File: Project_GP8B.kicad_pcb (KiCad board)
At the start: 4 copper layers, 133 x 93 mm, 103 parts, among them IC1 XC2C256-VQ100, J1 ALU_JTAG, J2 TE_Eurocard_96pole, J3 5530843-2, J4 UnusedPins_Connector, J5 ALU_PINS, U1 74AHC05, U10 74AHC1G04, U11 CD74AC238, U12 74AHC1G04, U13 CD74AC238, U14 74AHC08, U15 CD74AC238, U16 74AHC08, U17 74AHC138, U18 74HC165, U19 74AHCT244, U2 74AHC05, U20 74AHCT244, U21 74AHCT244, U22 74AHCT244, U23 74AHCT244, U24 74AHC273, U25 74AHCT595, U26 74AHC273, U27 74AHC273, U28 TPS7A0518PDBZR, U29 74AHC273, U3 74AHC1G04, U30 SN74LVC8T245DW, U31 74AHC273, U32 SN74AVC4T245D, U33 74AHC273, U35 74AHC273, U36 74AHC1G04, U37 74AHC273, U38 74AHC374, U39 74AHC1G04, U4 74AHC1G04, U5 74AHC05, U6 74AHC273, U7 74AHCT273, U8 74HC163, U9 CD74AC238

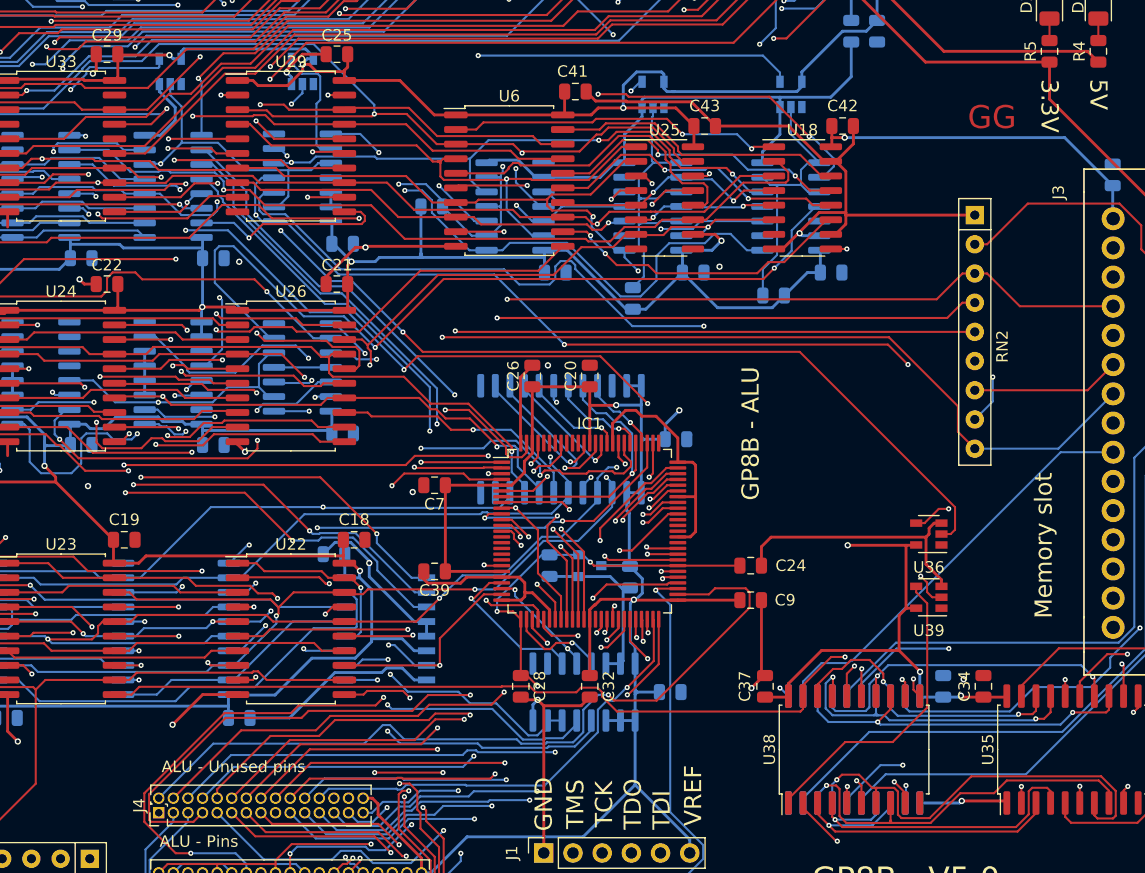
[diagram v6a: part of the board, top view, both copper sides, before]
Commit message: Apply MM1 memory standard, and shared power pin symbol fix
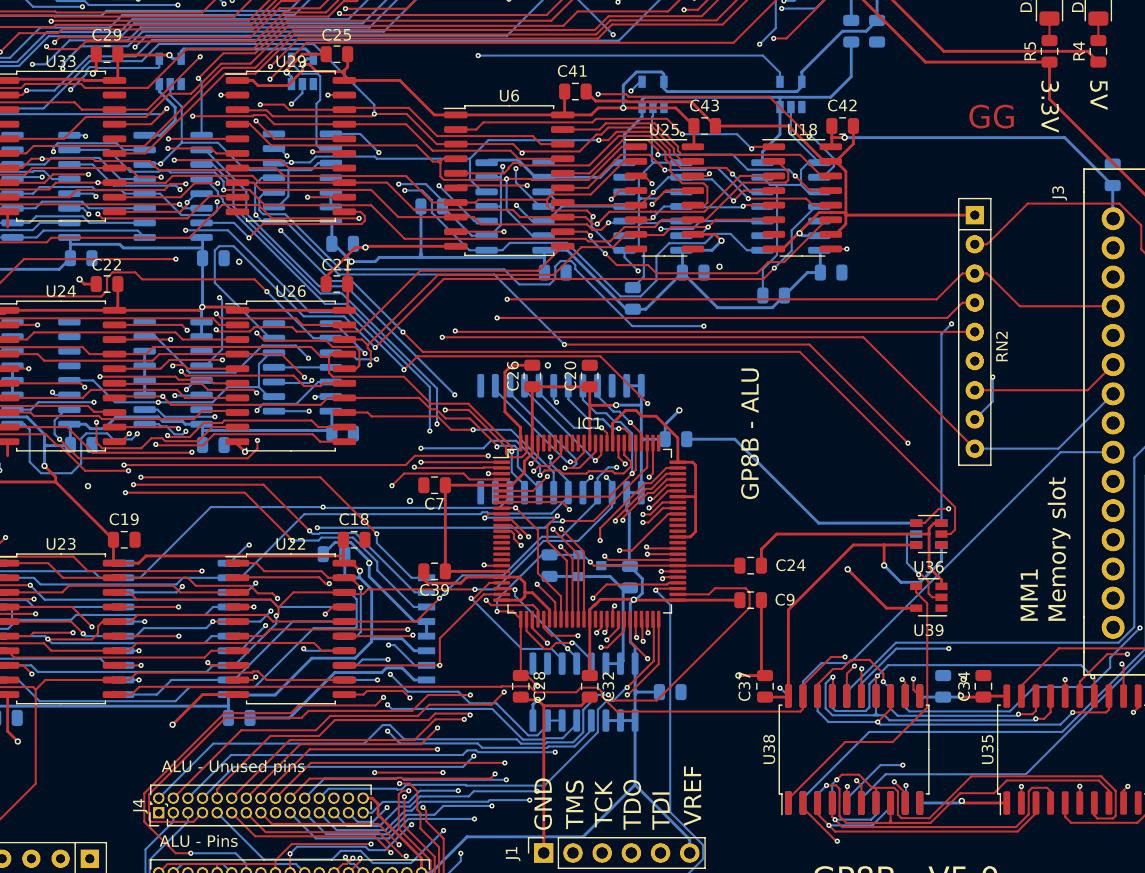
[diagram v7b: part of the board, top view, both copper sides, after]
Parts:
- removed G***: LOGO, QRCode:QRCode
- added U34: 74LVC1G34, Package_TO_SOT_SMD:SOT-23-5, B.Cu at (168.5, 89.8)
- J3: value 5530843-2 -> MM1_5530843-2
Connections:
- C34 pad 1: +5V -> +3V3
- C35 pad 1: +5V -> +3V3
- C37 pad 2: +5V -> +3V3
- J3 pad 27: /RAM_OE_CONTROL -> /RAM/B_RAM_~OE
- U35 pad 1: +5V -> +3V3
- U35 pad 20: +5V -> +3V3
- U36 pad 5: +5V -> +3V3
- U37 pad 1: +5V -> +3V3
- U37 pad 20: +5V -> +3V3
- U38 pad 20: +5V -> +3V3
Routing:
- net +3V3: track 238.9 -> 337.7 mm, vias 3 -> 6
- net +5V: track 660.9 -> 610.3 mm, vias 13 -> 10
- net /RAM/B_RAM_~OE: track 0.00 -> 43.5 mm, vias 0 -> 1
- net /RAM_OE_CONTROL: track 158.4 -> 128.7 mm
- net GND: track 410.5 -> 436.5 mm
- net /NumberSelect/RAMDATA_0: track 160.5 -> 159.2 mm
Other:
- board text added: "MM1 Memory slot"
- board text removed: "Memory slot"

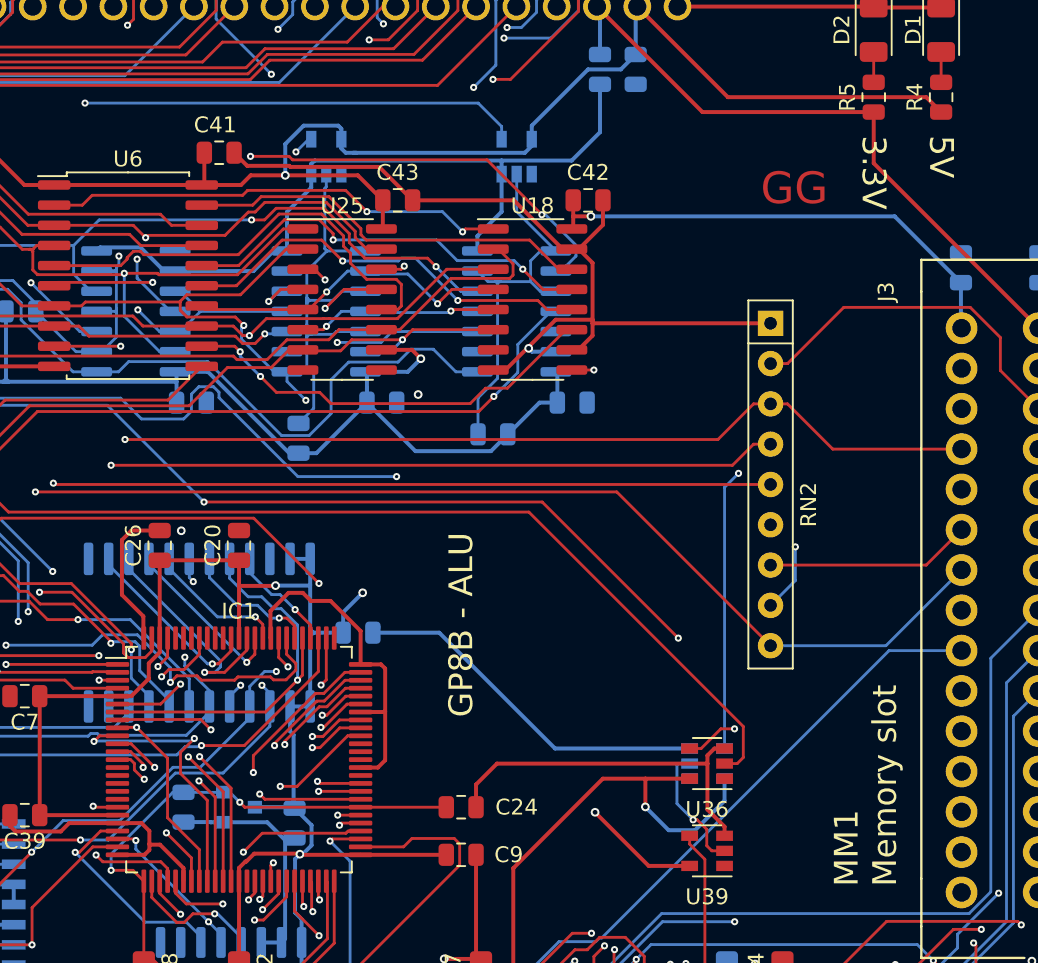
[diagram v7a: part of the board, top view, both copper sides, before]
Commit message: Revert SPI 4bits problem work-around (finally this fixed nothing)
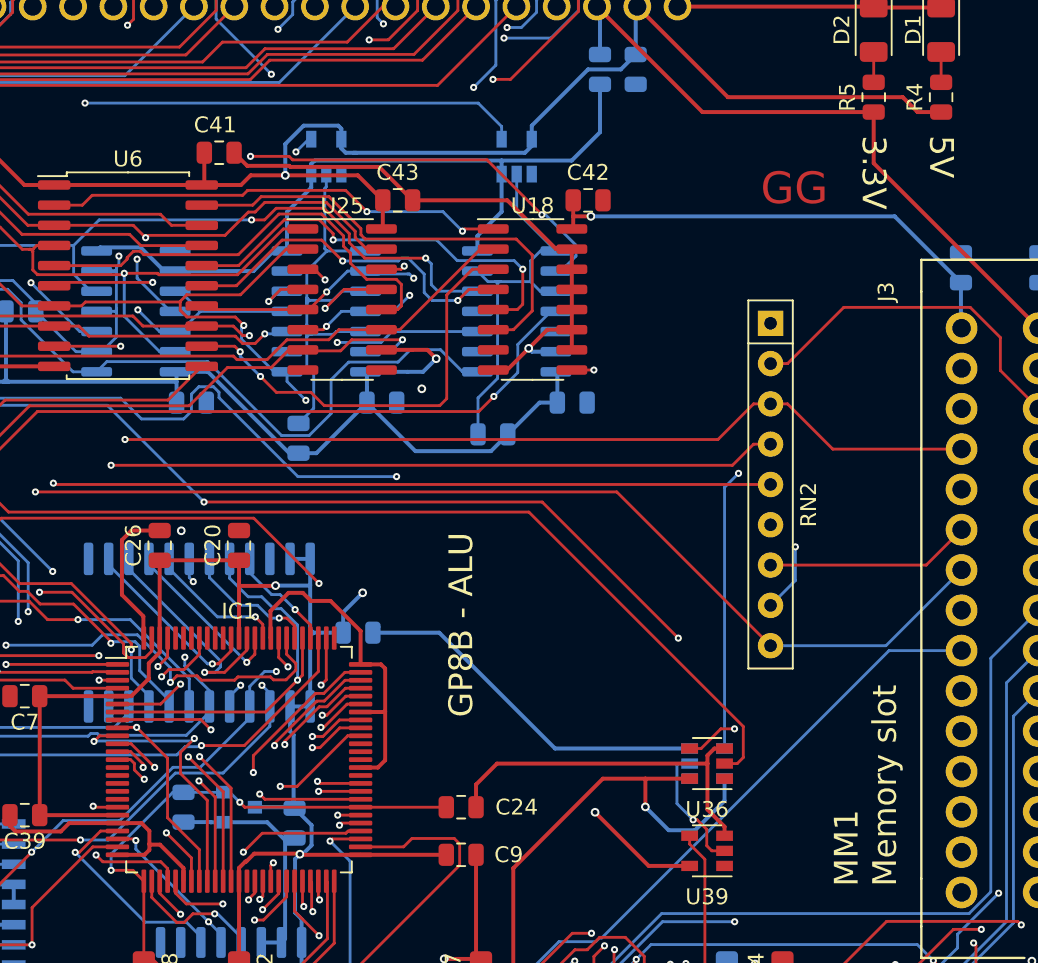
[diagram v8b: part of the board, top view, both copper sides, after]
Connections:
- U18 pad 11: /SPI/BUFF_0 -> GND
- U18 pad 12: /SPI/BUFF_1 -> GND
- U18 pad 13: /SPI/BUFF_2 -> GND
- U18 pad 14: /SPI/BUFF_3 -> GND
- U18 pad 3: /NUMBER_4 -> /SPI/BUFF_0
- U18 pad 4: /NUMBER_5 -> /SPI/BUFF_1
- U18 pad 5: /NUMBER_6 -> /SPI/BUFF_2
- U18 pad 6: /NUMBER_7 -> /SPI/BUFF_3
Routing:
- net /NUMBER_4: track 397.7 -> 380.6 mm
- net GND: track 436.5 -> 420.0 mm
- net /NUMBER_6: track 388.8 -> 381.5 mm
- net /NUMBER_7: track 413.6 -> 407.7 mm
- net /NUMBER_5: track 384.4 -> 379.5 mm
- net /SPI/BUFF_1: track 26.5 -> 22.3 mm
- net /SPI/BUFF_3: track 25.7 -> 29.3 mm
- net /SPI_CLK: track 70.9 -> 68.0 mm
- net +5V: track 610.3 -> 611.2 mm
- net /END_MAXCOUNT: track 71.4 -> 72.2 mm
- net /SPI/BUFF_2: track 26.6 -> 27.2 mm
- net /SPI/BUFF_0: track 26.9 -> 27.5 mm
